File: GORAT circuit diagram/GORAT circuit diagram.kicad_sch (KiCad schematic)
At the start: 79 parts, among them J1 AudioJack2, J2 AudioJack2, J3 Conn_01x08_Socket, J4 Conn_01x08_Socket, J6 Barrel_Jack, J8 Conn_01x02_Socket, J9 Conn_01x02_Socket, Q1 J111, SW1 SW_DPDT_x2, SW8 SW_Rotary2x6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

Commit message: update board and layout
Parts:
- removed SP3, SP4: Conn_01x02_Socket, Connector_PinHeader_2.54mm:PinHeader_1x02_P2.54mm_Vertical, symbol Connector:Conn_01x02_Socket
- renumbered RV4-BLEND2 to RV2-TILT1

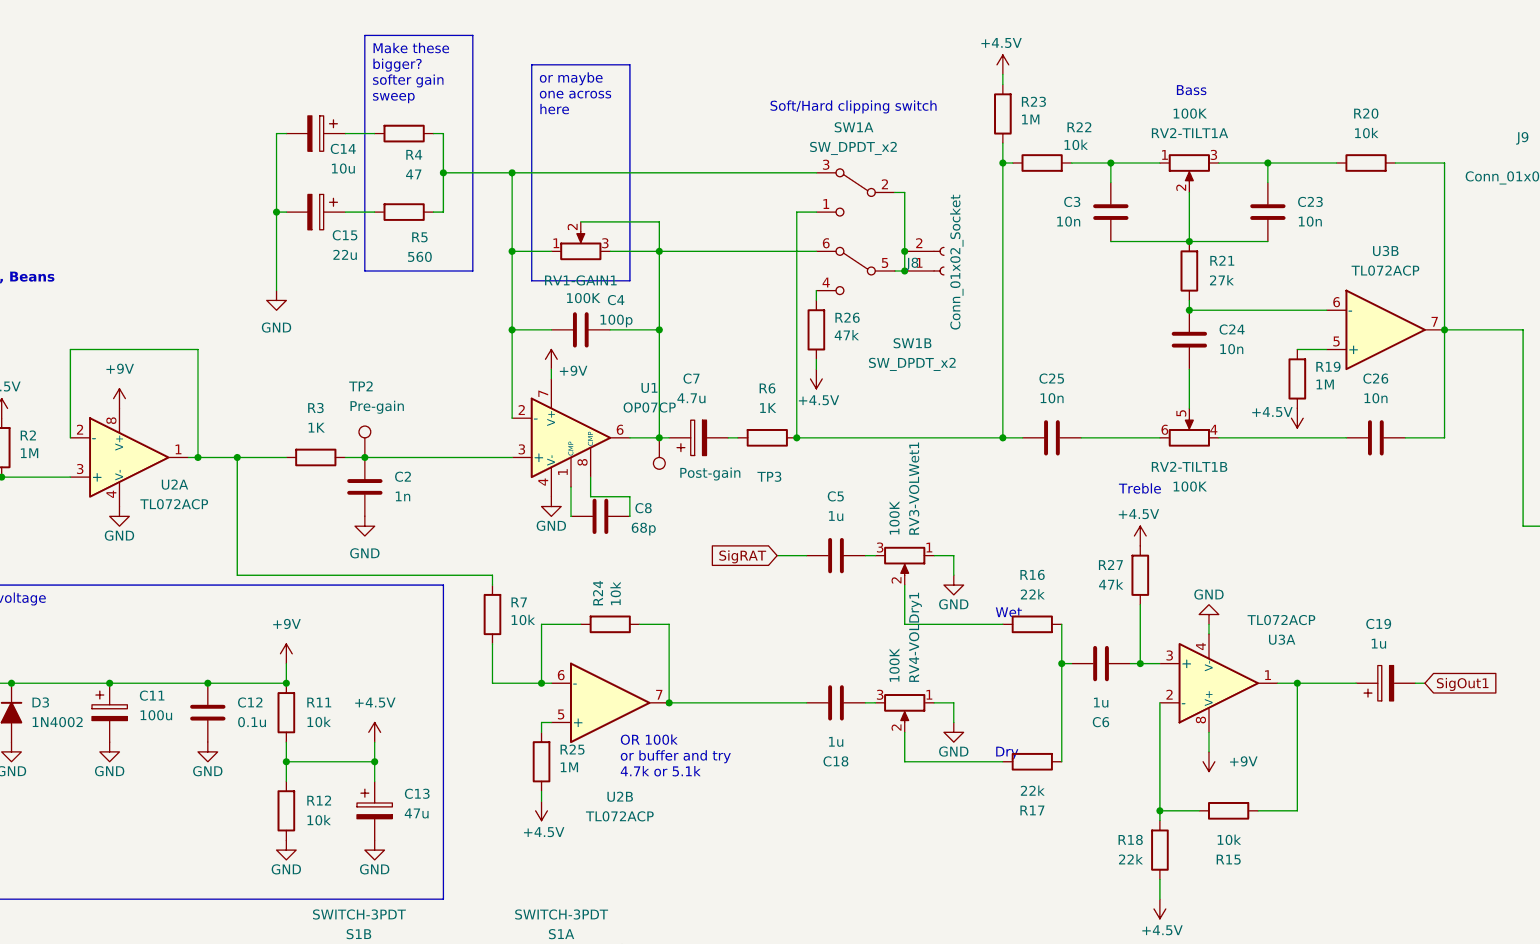
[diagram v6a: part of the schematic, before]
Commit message: Update KiCad files: remap nets and rename caps
Synchronise PCB and schematic: remap many net indices across GORAT circuit diagram (.kicad_pcb, .kicad_sch, .kicad_prl, .kicad_pro) to match the schematic, and rename several capacitor references (e.g. C7/C15/C19 -> Cp7/Cp15/Cp19). Add autosave and CSV export files, update GoRAT spreadsheet, and refresh backup ZIPs (deleted older backups, added new ones). These changes ensure net and reference consistency between schematic and board files.
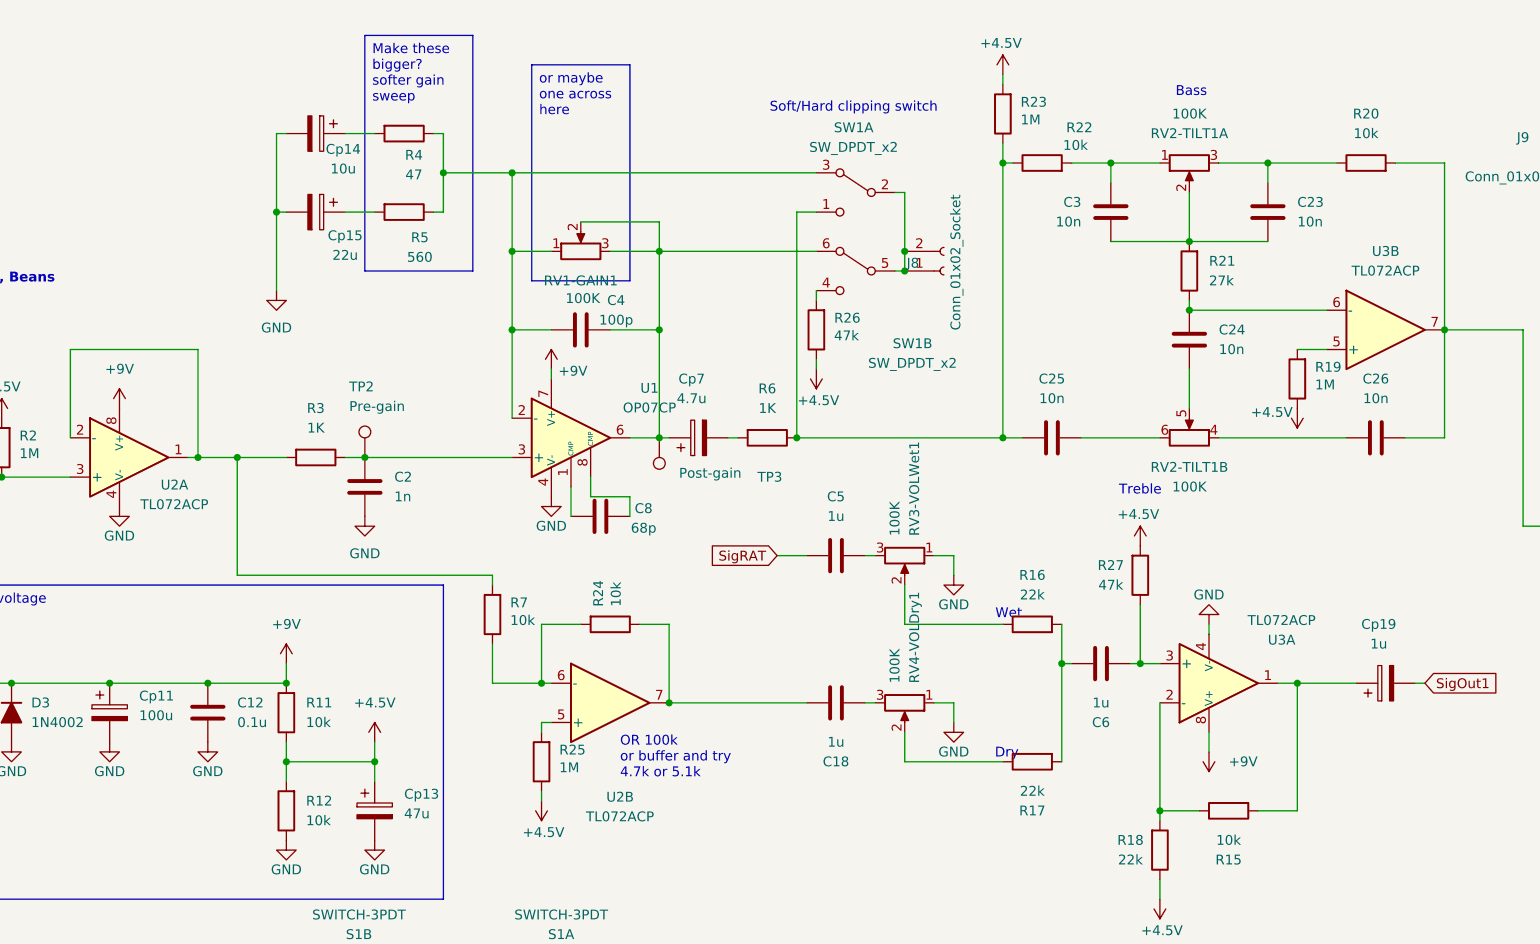
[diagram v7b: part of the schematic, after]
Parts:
- renumbered C11 to Cp11, C13 to Cp13, C14 to Cp14, C15 to Cp15, C19 to Cp19, C7 to Cp7
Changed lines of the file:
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@@
 		(dnp no)
 		(fields_autoplaced yes)
-		(property "Reference" "C13"
+		(property "Reference" "Cp13"
 			(at 86.36 118.4909 0)
 			(effects
@@
 			(project "GORAT circuit diagram"
 				(path "/5cc94095-982d-43d1-acd4-ea825b0c1010"
-					(reference "C13")
+					(reference "Cp13")
 					(unit 1)
 				)
@@
 		(on_board yes)
 		(dnp no)
-		(property "Reference" "C15"
+		(property "Reference" "Cp15"
 			(at 78.74 46.228 90)
 			(effects
@@
 			(project "GORAT circuit diagram"
 				(path "/5cc94095-982d-43d1-acd4-ea825b0c1010"
-					(reference "C15")
+					(reference "Cp15")
 					(unit 1)
 				)
@@
 		(dnp no)
 		(fields_autoplaced yes)
-		(property "Reference" "C7"
+		(property "Reference" "Cp7"
 			(at 123.571 64.77 90)
 			(effects
@@
 			(project "GORAT circuit diagram"
 				(path "/5cc94095-982d-43d1-acd4-ea825b0c1010"
-					(reference "C7")
+					(reference "Cp7")
 					(unit 1)
 				)
@@
 		(on_board yes)
 		(dnp no)
-		(property "Reference" "C14"
+		(property "Reference" "Cp14"
 			(at 78.486 35.052 90)
 			(effects
@@
 			(project "GORAT circuit diagram"
 				(path "/5cc94095-982d-43d1-acd4-ea825b0c1010"
-					(reference "C14")
+					(reference "Cp14")
 					(unit 1)
 				)
@@
 		(dnp no)
 		(fields_autoplaced yes)
-		(property "Reference" "C19"
+		(property "Reference" "Cp19"
 			(at 212.471 96.52 90)
 			(effects
@@
 			(project "GORAT circuit diagram"
 				(path "/5cc94095-982d-43d1-acd4-ea825b0c1010"
-					(reference "C19")
+					(reference "Cp19")
 					(unit 1)
 				)
@@
 		(on_board yes)
 		(dnp no)
-		(property "Reference" "C11"
+		(property "Reference" "Cp11"
 			(at 52.07 105.7909 0)
 			(effects
@@
 			(project "GORAT circuit diagram"
 				(path "/5cc94095-982d-43d1-acd4-ea825b0c1010"
-					(reference "C11")
+					(reference "Cp11")
 					(unit 1)
 				)

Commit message: V0.2 finished
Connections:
- net at SW8.3, SW8.4: now also D2.2 (A); no longer D8.2 (A)
- net at SW8.1, SW8.2: now also D8.2 (A); no longer D2.2 (A)
- net at J8.1 (Pin_1), SW1.5 (B): no longer J8.2 (Pin_2), SW1.2 (B)
- net at D1.1 (K), SW8.12, SW8.7: now also D7.1 (K)
- net at SW8.8, SW8.9: no longer D7.1 (K)
- new net: J8.2 (Pin_2), SW1.2 (B)
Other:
- note removed: "Bass, Reg, Beans"
- moved on the sheet: C12, Cp11, Cp13, D1, D2, D3, D7, D8, J8, R11, R12, R24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
